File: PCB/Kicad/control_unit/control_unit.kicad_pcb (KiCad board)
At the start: 6 copper layers, 150 x 150 mm, 82 parts, among them J1 in, J2 in, J3 in, J4 in, J5 in, J6 in, J7 in, J8 in, SW1 SW_Push, U4 7408, U57 744067

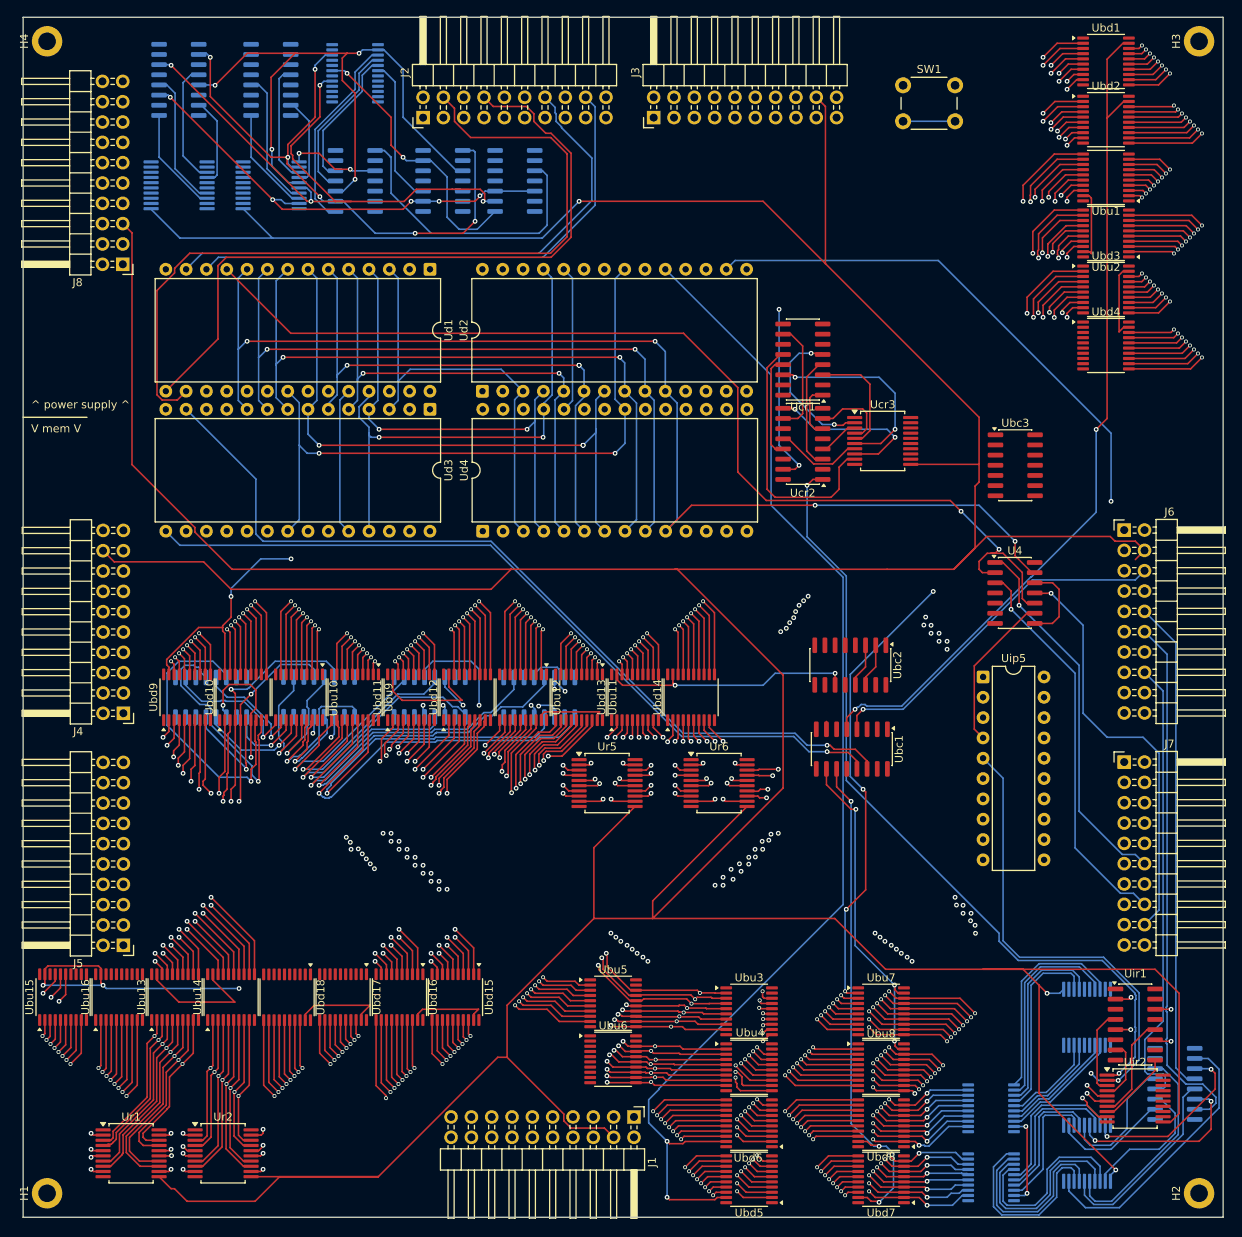
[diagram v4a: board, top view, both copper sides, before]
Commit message: CU routing mostly done, a bunch of control signals left
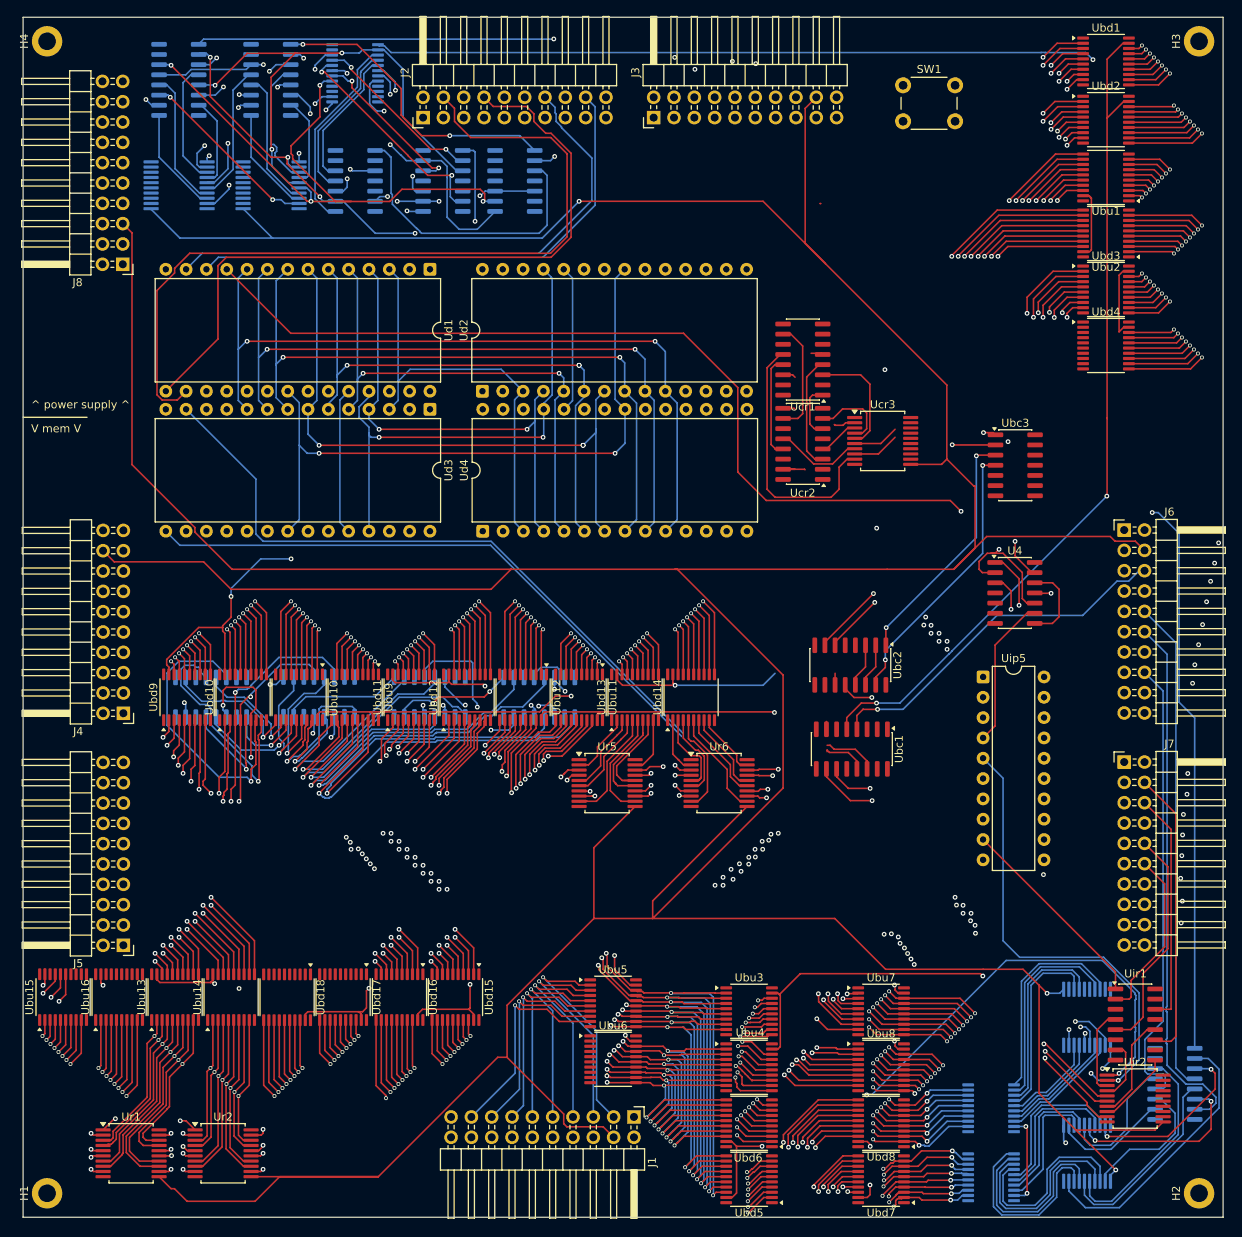
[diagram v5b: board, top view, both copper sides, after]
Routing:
- net /ioid2: track 85.5 -> 268.1 mm, vias 2 -> 4
- net /ControlUnit/should_jump: track 0.00 -> 179.8 mm, vias 0 -> 1
- net /ioid1: track 90.1 -> 247.5 mm, vias 2 -> 3
- net /ioid0: track 148.4 -> 302.9 mm
- net /ControlUnit/~{instr_load}: track 0.00 -> 144.9 mm, vias 0 -> 3
- net /ControlUnit/regds: track 0.00 -> 126.9 mm, vias 0 -> 1
- net /ControlUnit/~{next_instr}: track 101.4 -> 227.0 mm, vias 2 -> 5
- net /ControlUnit/ip/~{membusen}: track 16.2 -> 134.9 mm, vias 0 -> 1
- net /alubus7: track 89.5 -> 206.1 mm
- net /ControlUnit/ip/~{intidbusen}: track 36.3 -> 152.8 mm
- net /alubus6: track 87.6 -> 204.0 mm
- net /alubus15: track 118.0 -> 231.8 mm
- net /alubus5: track 84.7 -> 197.5 mm
- net /alubus14: track 117.3 -> 228.6 mm
- net /alubus4: track 85.0 -> 196.0 mm
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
